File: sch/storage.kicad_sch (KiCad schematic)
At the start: 5 parts, among them U3 74HC126

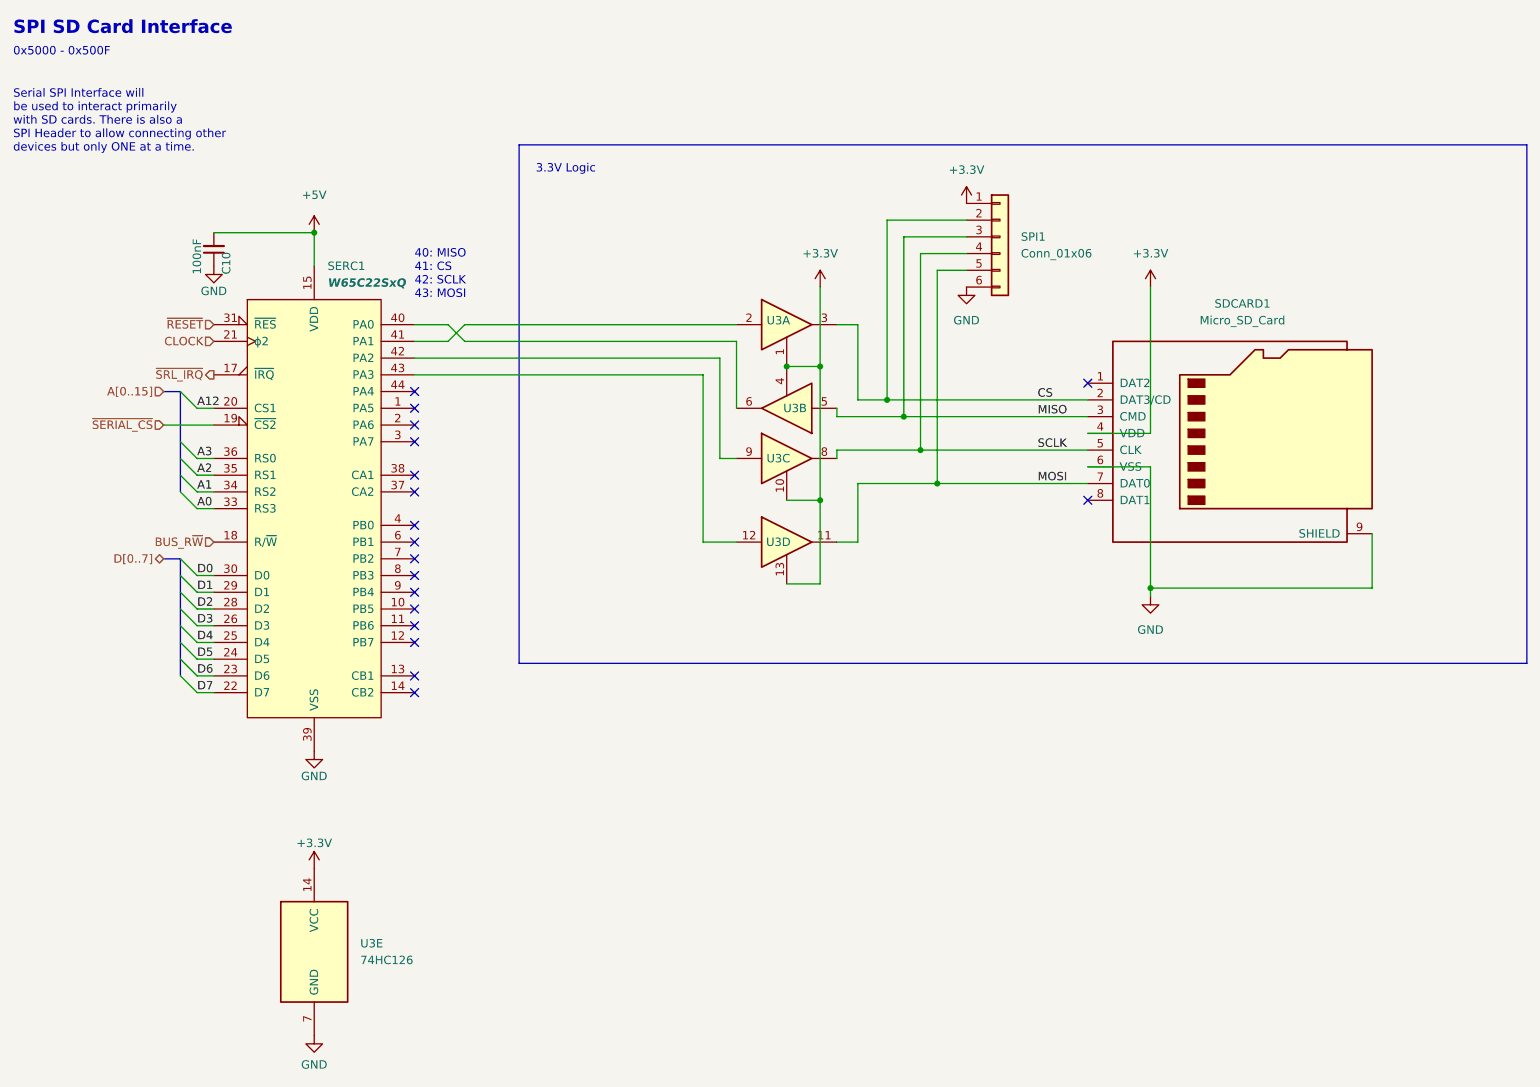
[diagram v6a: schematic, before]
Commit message: Comments in Sch
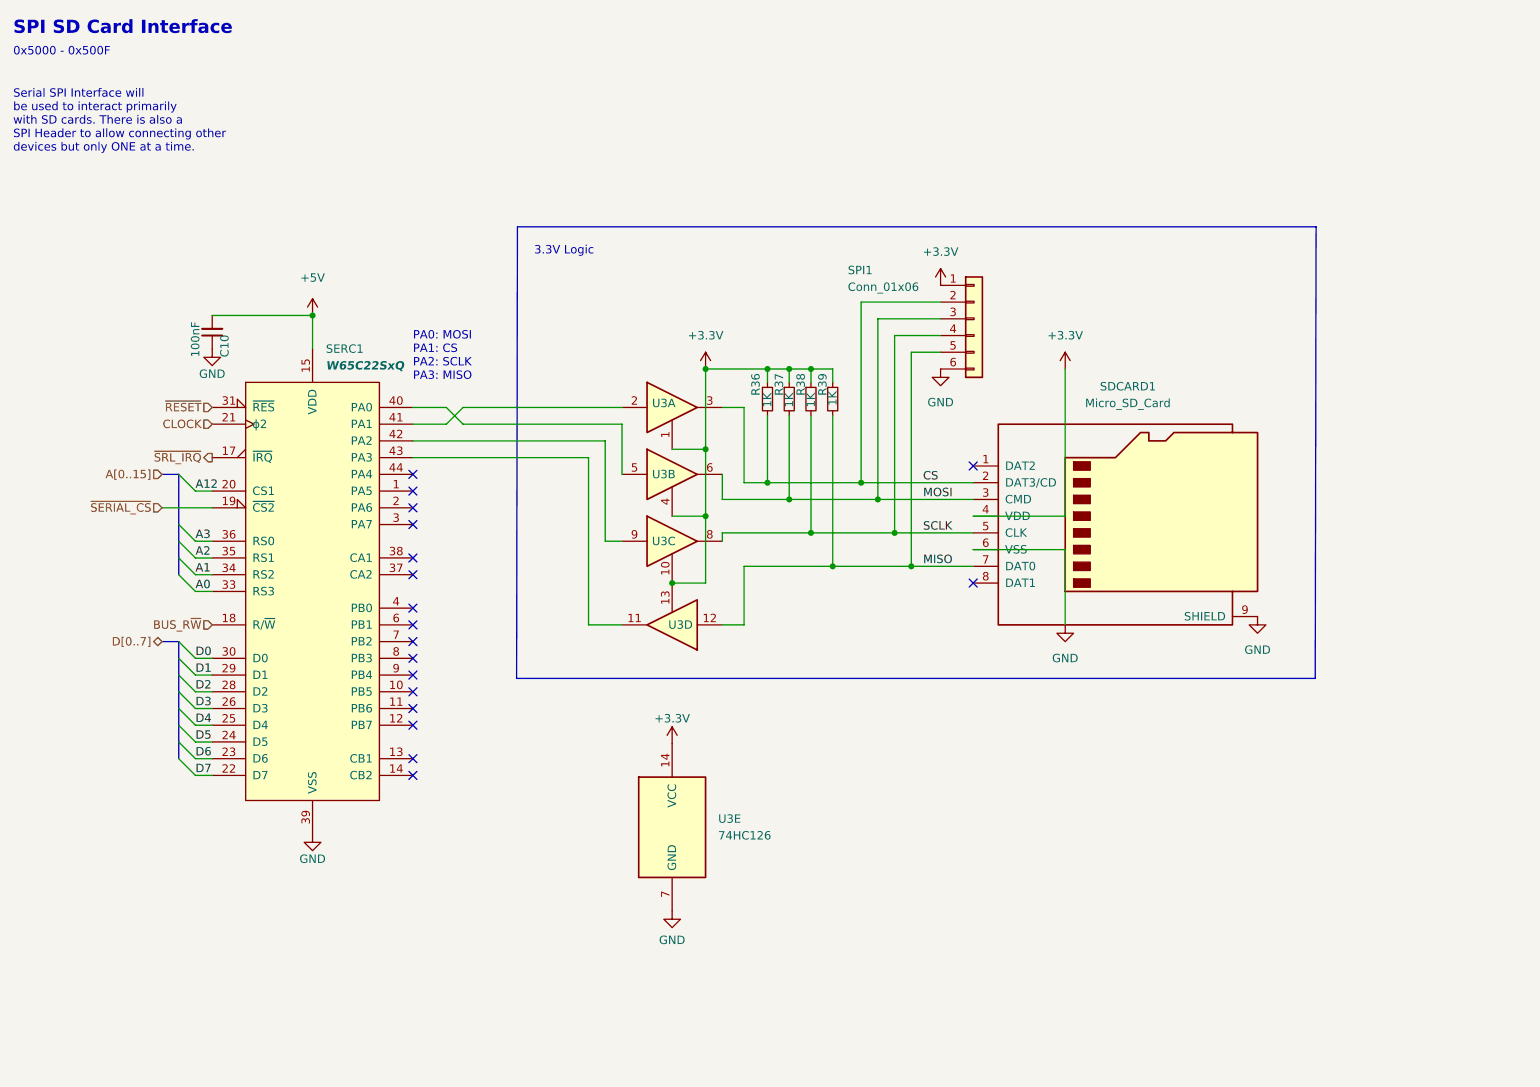
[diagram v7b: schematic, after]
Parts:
- added R36, R37, R38, R39: 1K, Resistor_SMD:R_0805_2012Metric, symbol Device:R_Small
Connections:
- net +3V3: now also R36.1, R37.1, R38.1, R39.1
- net CS: now also R36.2
- net MISO: now also SDCARD1.7 (DAT0), SPI1.5 (Pin_5), U3.12, R39.2; no longer SDCARD1.3 (CMD), SPI1.3 (Pin_3), U3.5
- net MOSI: now also SDCARD1.3 (CMD), SPI1.3 (Pin_3), U3.6, R37.2; no longer SDCARD1.7 (DAT0), SPI1.5 (Pin_5), U3.11
- net SCLK: now also R38.2
- net at SERC1.43 (PA3): now also U3.11; no longer U3.12
- net at SERC1.40 (PA0): now also U3.5; no longer U3.6
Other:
- note added: "PA0: MOSI PA1: CS PA2: SCLK PA3: MISO"
- note removed: "40: MISO 41: CS 42: SCLK 43: MOSI"
- moved on the sheet: C10, SDCARD1, SERC1, SPI1, U3A, U3B, U3C, U3D, U3E

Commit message: improve routing
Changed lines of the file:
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@@
     (stroke (width 0) (type default) (color 0 0 0 0))
   )
-  (wire (pts (xy 166.243 68.326) (xy 154.178 68.326))
+  (wire (pts (xy 166.37 68.326) (xy 154.178 68.326))
     (stroke (width 0) (type default) (color 0 0 0 0))
   )
@@
     (stroke (width 0) (type default) (color 0 0 0 0))
   )
-  (wire (pts (xy 166.243 73.406) (xy 159.258 73.406))
+  (wire (pts (xy 166.37 73.406) (xy 159.258 73.406))
     (stroke (width 0) (type default) (color 0 0 0 0))
   )
@@
     (stroke (width 0) (type default) (color 0 0 0 0))
   )
-  (polyline (pts (xy 101.981 56.896) (xy 223.266 56.896))
+  (polyline (pts (xy 102.108 56.896) (xy 223.266 56.896))
     (stroke (width 0) (type default) (color 0 0 0 0))
   )
@@
     (stroke (width 0) (type default) (color 0 0 0 0))
   )
-  (polyline (pts (xy 101.981 56.896) (xy 101.854 125.476))
+  (polyline (pts (xy 102.108 56.896) (xy 101.854 125.476))
     (stroke (width 0) (type default) (color 0 0 0 0))
   )
@@
     (stroke (width 0) (type default) (color 0 0 0 0))
   )
-  (polyline (pts (xy 223.139 125.476) (xy 223.266 56.896))
+  (polyline (pts (xy 223.266 125.476) (xy 223.266 56.896))
     (stroke (width 0) (type default) (color 0 0 0 0))
   )
@@
     (stroke (width 0) (type default) (color 0 0 0 0))
   )
-  (polyline (pts (xy 101.854 125.476) (xy 223.139 125.476))
-    (stroke (width 0) (type default) (color 0 0 0 0))
-  )
-  (wire (pts (xy 166.243 75.946) (xy 161.798 75.946))
+  (polyline (pts (xy 101.854 125.476) (xy 223.266 125.476))
+    (stroke (width 0) (type default) (color 0 0 0 0))
+  )
+  (wire (pts (xy 166.37 75.946) (xy 161.798 75.946))
     (stroke (width 0) (type default) (color 0 0 0 0))
   )
@@
     (stroke (width 0) (type default) (color 0 0 0 0))
   )
-  (wire (pts (xy 166.243 70.866) (xy 156.718 70.866))
+  (wire (pts (xy 166.37 70.866) (xy 156.718 70.866))
     (stroke (width 0) (type default) (color 0 0 0 0))
   )
@@
     (pin "1")
   )
-  (symbol (lib_id "power:GND") (at 166.243 78.486 0) (unit 1)
-    (in_bom yes) (on_board yes) (fields_autoplaced)
-    (property "Reference" "#PWR0109" (id 0) (at 166.243 84.836 0)
-      (effects (font (size 1.27 1.27)) hide)
-    )
-    (property "Value" "GND" (id 1) (at 166.243 83.566 0))
-    (property "Footprint" "" (id 2) (at 166.243 78.486 0)
-      (effects (font (size 1.27 1.27)) hide)
-    )
-    (property "Datasheet" "" (id 3) (at 166.243 78.486 0)
+  (symbol (lib_id "power:GND") (at 166.37 78.486 0) (unit 1)
+    (in_bom yes) (on_board yes) (fields_autoplaced)
+    (property "Reference" "#PWR0109" (id 0) (at 166.37 84.836 0)
+      (effects (font (size 1.27 1.27)) hide)
+    )
+    (property "Value" "GND" (id 1) (at 166.37 83.566 0))
+    (property "Footprint" "" (id 2) (at 166.37 78.486 0)
+      (effects (font (size 1.27 1.27)) hide)
+    )
+    (property "Datasheet" "" (id 3) (at 166.37 78.486 0)
       (effects (font (size 1.27 1.27)) hide)
     )
@@
     (pin "7")
   )
-  (symbol (lib_id "Connector_Generic:Conn_01x06") (at 171.323 70.866 0) (unit 1)
-    (in_bom yes) (on_board yes)
-    (property "Reference" "SPI1" (id 0) (at 152.146 63.5 0)
-      (effects (font (size 1.27 1.27)) (justify left))
-    )
-    (property "Value" "Conn_01x06" (id 1) (at 152.146 66.04 0)
-      (effects (font (size 1.27 1.27)) (justify left))
-    )
-    (property "Footprint" "Connector_PinHeader_2.54mm:PinHeader_1x06_P2.54mm_Vertical" (id 2) (at 171.323 70.866 0)
-      (effects (font (size 1.27 1.27)) hide)
-    )
-    (property "Datasheet" "~" (id 3) (at 171.323 70.866 0)
+  (symbol (lib_id "Connector_Generic:Conn_01x06") (at 171.45 70.866 0) (unit 1)
+    (in_bom yes) (on_board yes)
+    (property "Reference" "SPI1" (id 0) (at 152.273 63.5 0)
+      (effects (font (size 1.27 1.27)) (justify left))
+    )
+    (property "Value" "Conn_01x06" (id 1) (at 152.273 66.04 0)
+      (effects (font (size 1.27 1.27)) (justify left))
+    )
+    (property "Footprint" "Connector_PinHeader_2.54mm:PinHeader_1x06_P2.54mm_Vertical" (id 2) (at 171.45 70.866 0)
+      (effects (font (size 1.27 1.27)) hide)
+    )
+    (property "Datasheet" "~" (id 3) (at 171.45 70.866 0)
       (effects (font (size 1.27 1.27)) hide)
     )
@@
     (pin "7")
   )
-  (symbol (lib_id "power:+3.3V") (at 166.243 65.786 0) (unit 1)
-    (in_bom yes) (on_board yes) (fields_autoplaced)
-    (property "Reference" "#PWR0108" (id 0) (at 166.243 69.596 0)
-      (effects (font (size 1.27 1.27)) hide)
-    )
-    (property "Value" "+3.3V" (id 1) (at 166.243 60.706 0))
-    (property "Footprint" "" (id 2) (at 166.243 65.786 0)
-      (effects (font (size 1.27 1.27)) hide)
-    )
-    (property "Datasheet" "" (id 3) (at 166.243 65.786 0)
-      (effects (font (size 1.27 1.27)) hide)
-    )
+  (symbol (lib_id "power:+3.3V") (at 166.37 65.786 0) (unit 1)
+    (in_bom yes) (on_board yes) (fields_autoplaced)
+    (property "Reference" "#PWR0108" (id 0) (at 166.37 69.596 0)
+      (effects (font (size 1.27 1.27)) hide)
+    )
+    (property "Value" "+3.3V" (id 1) (at 166.37 60.706 0))
+    (property "Footprint" "" (id 2) (at 166.37 65.786 0)
+      (effects (font (size 1.27 1.27)) hide)
+    )
+    (property "Datasheet" "" (id 3) (at 166.37 65.786 0)
+      (effects (font (size 1.27 1.27)) hide)
+    )
